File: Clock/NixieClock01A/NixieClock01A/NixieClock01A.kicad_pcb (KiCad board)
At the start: 2 copper layers, 17 parts, among them U1 74141, U2 PCF8574, U3 ESP-12E

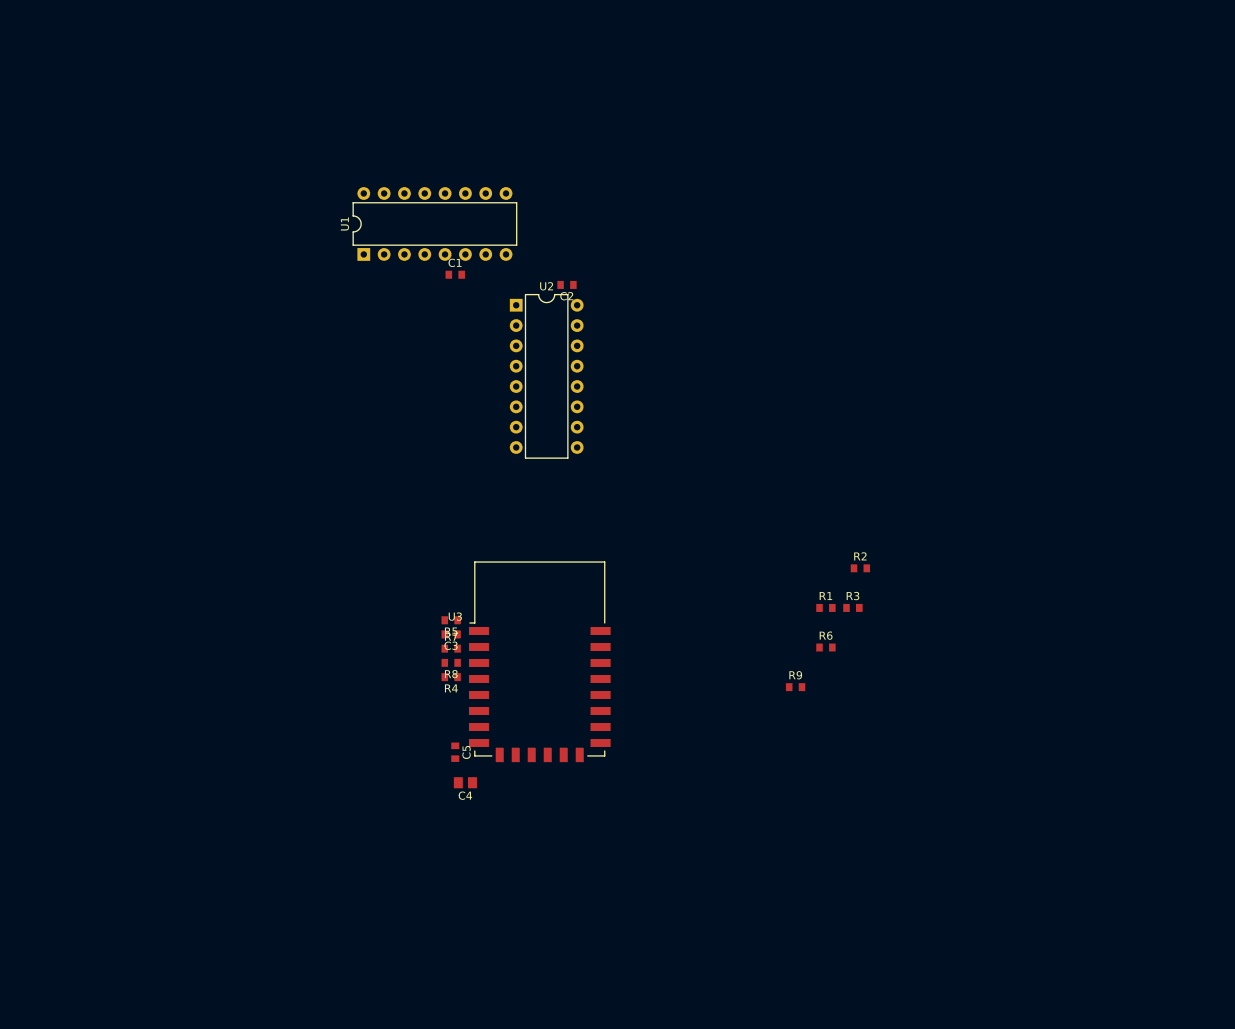
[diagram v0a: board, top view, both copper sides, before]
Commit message: LM3478, ESP8266 layout
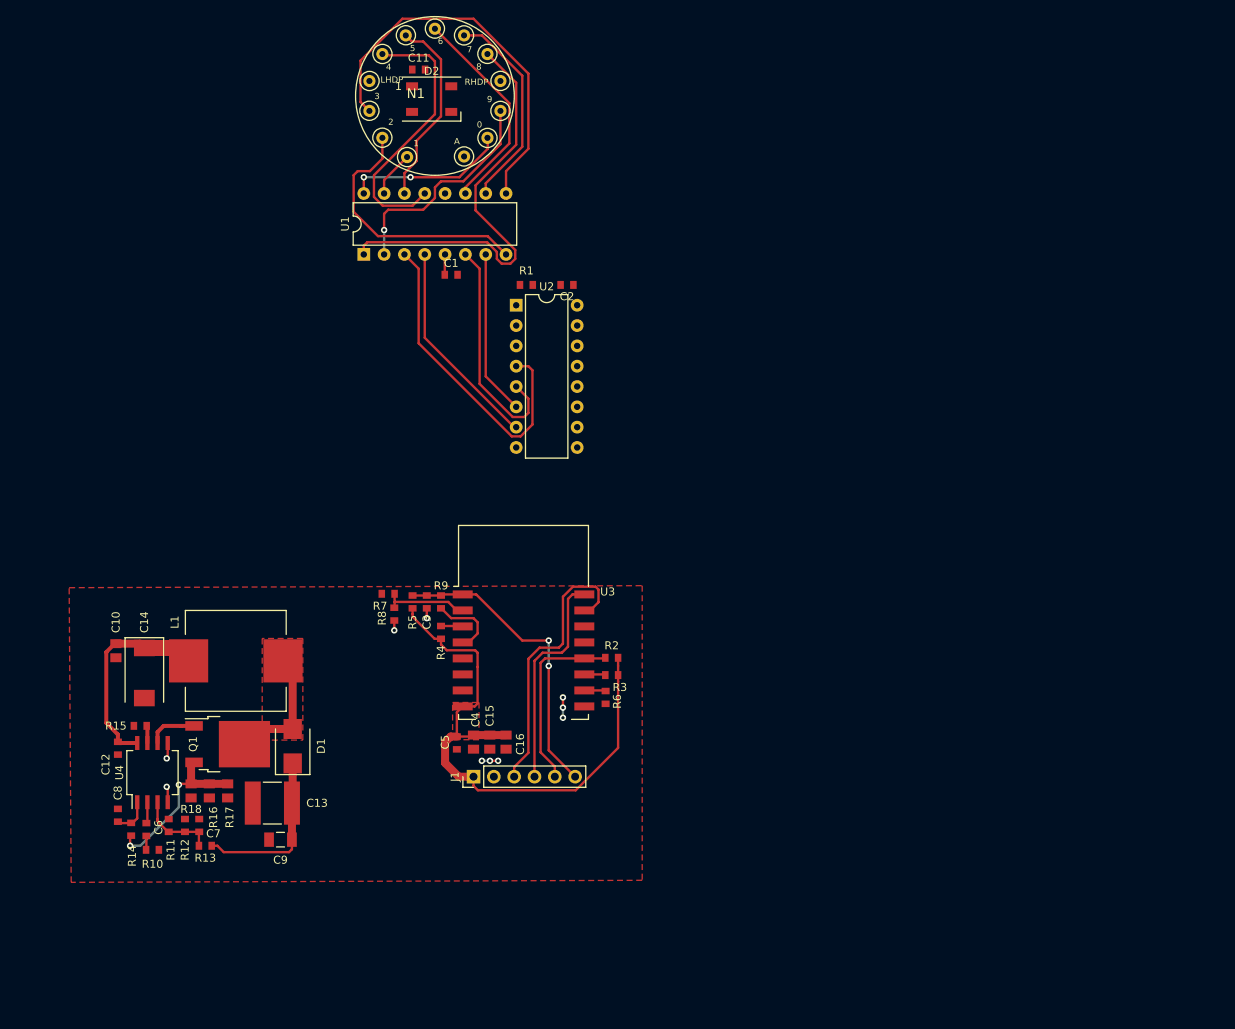
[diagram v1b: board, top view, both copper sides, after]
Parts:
- added C10: 10u, Capacitor_SMD:C_0805_2012Metric, F.Cu at (87.1, 106.7)
- added C11: 100n, Capacitor_SMD:C_0603_1608Metric, F.Cu at (125.0, 34.0)
- added C12: 100n, Capacitor_SMD:C_0603_1608Metric, F.Cu at (87.4, 118.9)
- added C13: 1u, Capacitor_SMD:C_2220_5650Metric, F.Cu at (106.7, 125.7)
- added C14: 100u, Capacitor_Tantalum_SMD:CP_EIA-7343-31_Kemet-D, F.Cu at (90.7, 109.5)
- added C15: 10u, Capacitor_SMD:C_0805_2012Metric, F.Cu at (133.9, 118.1)
- added C16: 10u, Capacitor_SMD:C_0805_2012Metric, F.Cu at (135.9, 118.1)
- added C6: 22n, Capacitor_SMD:C_0603_1608Metric, F.Cu at (90.9, 129.0)
- added C7: 22n, Capacitor_SMD:C_0603_1608Metric, F.Cu at (97.5, 128.5)
- added C8: C, Capacitor_SMD:C_0603_1608Metric, F.Cu at (87.4, 127.3)
- added C9: 100n, Capacitor_SMD:C_1206_3216Metric, F.Cu at (107.7, 130.3)
- added D1: D_Schottky, Diode_SMD:D_SMB, F.Cu at (109.2, 118.6)
- added D2: WS2812B, LED_SMD:LED_WS2812B_PLCC4_5.0x5.0mm_P3.2mm, F.Cu at (126.6, 37.7)
- added J1: Conn_01x06_Male, Connector_PinHeader_2.54mm:PinHeader_1x06_P2.54mm_Vertical, F.Cu at (131.8, 122.4)
- added L1: L_Core_Ferrite, Inductor_SMD:L_Wuerth_WE-PD-Typ-LS_Handsoldering, F.Cu at (102.1, 108.0)
- added N1: ZM1080, zm1080:ZM1080, F.Cu at (127.0, 37.3)
- added Q1: Q_NMOS_GDS, Package_TO_SOT_SMD:TO-252-2, F.Cu at (101.1, 118.4)
- added R10: 4k7, Resistor_SMD:R_0603_1608Metric, F.Cu at (91.7, 131.6)
- added R11: R, Resistor_SMD:R_0603_1608Metric, F.Cu at (93.7, 128.5)
- added R12: R, Resistor_SMD:R_0603_1608Metric, F.Cu at (95.8, 128.5)
- added R13: R, Resistor_SMD:R_0603_1608Metric, F.Cu at (98.3, 131.1)
- added R14: R, Resistor_SMD:R_0603_1608Metric, F.Cu at (89.0, 129.0)
- added R15: 40k, Resistor_SMD:R_0603_1608Metric, F.Cu at (90.2, 116.1)
- added R16: R, Resistor_SMD:R_0805_2012Metric, F.Cu at (98.8, 124.2)
- added R17: R, Resistor_SMD:R_0805_2012Metric, F.Cu at (101.1, 124.2)
- added R18: R, Resistor_SMD:R_0805_2012Metric, F.Cu at (96.5, 124.2)
- added U4: LM3478, Package_SO:SO-8_5.3x6.2mm_P1.27mm, F.Cu at (91.7, 121.9)
- U3: footprint RF_Module:ESP-12E -> riske-lib:ESP-12E
- moved R1 55.1 mm to (138.4, 61.0), turned to 180 degrees
- moved R9 45.6 mm to (127.8, 100.6), turned to 270 degrees
- moved R2 33.0 mm to (149.1, 107.6)
- moved R3 31.3 mm to (149.1, 109.7)
- moved R6 28.2 mm to (148.3, 112.5), turned to 270 degrees
- moved R7 10.4 mm to (121.2, 99.6)
- moved R8 9.37 mm to (121.9, 102.1), turned to 270 degrees
- moved R4 5.73 mm to (127.8, 104.4), turned to 270 degrees
- moved R5 5.34 mm to (124.2, 100.6), turned to 270 degrees
- moved C4 5.18 mm to (131.8, 118.1), turned to 270 degrees
- moved C3 5.08 mm to (126.0, 100.6), turned to 270 degrees
- moved U3 5.00 mm to (138.1, 103.1)
- moved C5 1.19 mm to (129.7, 118.2)
- moved C1 0.51 mm to (129.0, 59.7)
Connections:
- U3 pad 21: Net-(U3-Pad21) -> /RX
- U3 pad 22: Net-(U3-Pad22) -> /TX
- U3 pad 7: Net-(U3-Pad7) -> /NeoPix1
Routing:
- net +3V3: track 0.00 -> 71.7 mm
- net Net-(N1-Pad9): track 0.00 -> 53.3 mm
- net Net-(N1-Pad3): track 0.00 -> 48.9 mm
- net /A1: track 0.00 -> 40.5 mm
- net /RST: track 0.00 -> 37.8 mm, vias 0 -> 2
- net /RX: track 0.00 -> 35.3 mm
- net Net-(N1-Pad5): track 0.00 -> 34.5 mm
- net Net-(N1-Pad2): track 0.00 -> 32.9 mm
- net /A2: track 0.00 -> 28.9 mm
- net +5V: track 0.00 -> 28.5 mm
- net Net-(N1-Pad11): track 0.00 -> 28.2 mm, vias 0 -> 1
- net /TX: track 0.00 -> 27.6 mm
- net Net-(N1-Pad7): track 0.00 -> 26.7 mm
- net /A4: track 0.00 -> 26.5 mm
- net Net-(N1-Pad8): track 0.00 -> 26.0 mm
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- added copper zone on F.Cu, net +3V3
- added copper zone on F.Cu, net GND
- added copper zone on F.Cu, net Net-(D1-Pad2)
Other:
- net class Default: trace_width 0.25 -> 0.2
- rule via_min_size: 0.4 -> 0.5

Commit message: Nixie layout
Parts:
- added C17: 100n, Capacitor_SMD:C_0603_1608Metric, B.Cu at (193.0, 83.2)
- added C18: 100n, Capacitor_SMD:C_0603_1608Metric, F.Cu at (139.0, 142.0)
- added C19: 100n, Capacitor_SMD:C_0603_1608Metric, F.Cu at (189.6, 62.8)
- added C20: 100n, Capacitor_SMD:C_0603_1608Metric, F.Cu at (158.8, 62.8)
- added C21: 100n, Capacitor_SMD:C_0603_1608Metric, F.Cu at (125.5, 142.0)
- added C22: 100n, Capacitor_SMD:C_0603_1608Metric, B.Cu at (162.2, 83.2)
- added C23: 100n, Capacitor_SMD:C_0603_1608Metric, F.Cu at (137.4, 62.8)
- added C24: 100n, Capacitor_SMD:C_0603_1608Metric, F.Cu at (106.2, 62.8)
- added C25: 10u, Capacitor_SMD:C_0805_2012Metric, F.Cu at (156.0, 119.8)
- added C26: 10u, Capacitor_SMD:C_0805_2012Metric, F.Cu at (146.0, 123.5)
- added C27: 100n, Capacitor_SMD:C_0603_1608Metric, B.Cu at (140.8, 83.2)
- added C28: 100n, Capacitor_SMD:C_0603_1608Metric, F.Cu at (84.8, 62.8)
- added C29: 100n, Capacitor_SMD:C_0603_1608Metric, F.Cu at (156.0, 123.2)
- added C30: 100n, Capacitor_SMD:C_0603_1608Metric, F.Cu at (146.0, 119.5)
- added C31: 100n, Capacitor_SMD:C_0603_1608Metric, B.Cu at (109.8, 83.2)
- added C32: 100n, Capacitor_SMD:C_0603_1608Metric, B.Cu at (88.2, 83.2)
- added D3: WS2812B, LED_SMD:LED_WS2812B_PLCC4_5.0x5.0mm_P3.2mm, F.Cu at (191.5, 66.4)
- added D4: WS2812B, LED_SMD:LED_WS2812B_PLCC4_5.0x5.0mm_P3.2mm, F.Cu at (161.0, 66.4)
- added D5: WS2812B, LED_SMD:LED_WS2812B_PLCC4_5.0x5.0mm_P3.2mm, F.Cu at (139.6, 66.5)
- added D6: WS2812B, LED_SMD:LED_WS2812B_PLCC4_5.0x5.0mm_P3.2mm, F.Cu at (108.5, 66.4)
- added D7: WS2812B, LED_SMD:LED_WS2812B_PLCC4_5.0x5.0mm_P3.2mm, F.Cu at (87.0, 66.4)
- added J2: Conn_02x16_Odd_Even, Connector_PinSocket_2.54mm:PinSocket_2x16_P2.54mm_Vertical, F.Cu at (170.0, 149.0)
- added J3: Conn_02x16_Odd_Even, Connector_PinSocket_2.54mm:PinSocket_2x16_P2.54mm_Vertical, F.Cu at (170.0, 97.0)
- added N2: ZM1080, riske-lib:ZM1080, F.Cu at (191.5, 66.3)
- added N3: ZM1080, riske-lib:ZM1080, F.Cu at (161.0, 66.3)
- added N4: ZM1080, riske-lib:ZM1080, F.Cu at (139.6, 66.4)
- added N5: ZM1080, riske-lib:ZM1080, F.Cu at (108.5, 66.3)
- added N6: ZM1080, riske-lib:ZM1080, F.Cu at (87.0, 66.3)
- added R19: R, Resistor_SMD:R_0603_1608Metric, F.Cu at (150.0, 140.0)
- added R20: R, Resistor_SMD:R_0603_1608Metric, F.Cu at (136.5, 140.0)
- added R21: 27k, Resistor_SMD:R_1206_3216Metric, B.Cu at (213.2, 75.0)
- added R22: 27k, Resistor_SMD:R_1206_3216Metric, B.Cu at (191.6, 75.0)
- added R23: 27k, Resistor_SMD:R_1206_3216Metric, B.Cu at (161.2, 75.0)
- added R24: 27k, Resistor_SMD:R_1206_3216Metric, B.Cu at (139.8, 75.2)
- added R25: 27k, Resistor_SMD:R_1206_3216Metric, B.Cu at (108.6, 75.0)
- added R26: 27k, Resistor_SMD:R_1206_3216Metric, B.Cu at (87.0, 75.0)
- added U10: L78L33_TO92, Package_TO_SOT_THT:TO-92_Inline, F.Cu at (149.9, 120.3)
- added U11: 74141, Package_DIP:DIP-16_W7.62mm, F.Cu at (130.6, 86.0)
- added U12: 74141, Package_DIP:DIP-16_W7.62mm, F.Cu at (99.5, 85.9)
- added U13: 74141, Package_DIP:DIP-16_W7.62mm, F.Cu at (78.0, 85.9)
- added U5: 74141, Package_DIP:DIP-16_W7.62mm, F.Cu at (182.8, 85.9)
- added U6: PCF8574, Package_SO:SOIC-16W_5.3x10.2mm_P1.27mm, F.Cu at (144.0, 136.0)
- added U7: PCF8574, Package_SO:SOIC-16W_5.3x10.2mm_P1.27mm, F.Cu at (130.5, 136.0)
- added U8: 74141, Package_DIP:DIP-16_W7.62mm, F.Cu at (152.0, 85.9)
- added U9: L78L05_TO92, Package_TO_SOT_THT:TO-92_Inline, F.Cu at (159.3, 120.0)
- C1: moved to B.Cu
- C13: value 1u -> 1u/200V
- C9: value 100n -> 100n/200V
- N1: footprint zm1080:ZM1080 -> riske-lib:ZM1080
- U2: footprint Package_DIP:DIP-16_W7.62mm -> Package_SO:SOIC-16W_5.3x10.2mm_P1.27mm
- U3: footprint riske-lib:ESP-12E -> RF_Module:ESP-12E
- moved C10 108.7 mm to (194.8, 121.4), turned to 180 degrees
- moved C14 102.5 mm to (192.0, 124.9), turned to 180 degrees
- moved L1 95.8 mm to (193.6, 136.4), turned to 270 degrees
- moved R15 95.6 mm to (185.4, 124.4), turned to 90 degrees
- moved C12 95.3 mm to (182.6, 121.6), turned to 180 degrees
- moved D2 91.0 mm to (213.0, 66.4)
- moved N1 90.7 mm to (213.0, 66.3)
- moved C11 90.7 mm to (211.0, 62.8)
- moved U1 90.7 mm to (204.1, 85.9)
- moved C1 88.4 mm to (214.3, 83.2), turned to 90 degrees
- moved U4 88.0 mm to (179.6, 125.9), turned to 0 degrees
- moved C8 87.1 mm to (174.2, 121.6), turned to 180 degrees
- moved Q1 83.8 mm to (183.1, 135.3), turned to 270 degrees
- moved R14 83.7 mm to (172.5, 123.3), turned to 0 degrees
- moved R1 82.8 mm to (163.0, 140.0), turned to 270 degrees
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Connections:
- net /NeoPix1 renamed /NeoPix
- C11 pad 1: +3V3 -> +5V
- D2 pad 1: +3V3 -> +5V
- J1 pad 1: +3V3 -> GND
- J1 pad 2: GND -> +3V3
- J1 pad 3: /RX -> /TX
- J1 pad 4: /TX -> /RX
- N1 pad 13: /Uanode -> Net-(N1-Pad13)
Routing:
- net +5V: track 28.5 -> 349.2 mm, vias 0 -> 6
- net /Uanode: track 21.3 -> 273.6 mm, vias 0 -> 1
- net /F3: track 0.00 -> 86.6 mm
- net /NeoPix: track 0.00 -> 85.3 mm, vias 0 -> 1
- net /F4: track 0.00 -> 80.0 mm
- net /F1: track 0.00 -> 74.3 mm
- net /E3: track 0.00 -> 73.7 mm
- net /F2: track 0.00 -> 72.6 mm
- net /E4: track 0.00 -> 68.8 mm
- net /B3: track 0.00 -> 67.7 mm
- net /B2: track 0.00 -> 66.3 mm
- net /A3: track 20.6 -> 83.2 mm
- net /B4: track 0.00 -> 62.5 mm
- net Net-(N2-Pad2): track 0.00 -> 55.2 mm
- net /A4: track 26.5 -> 81.4 mm
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- added copper zone on B.Cu, net GND
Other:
- net class Default: trace_width 0.2 -> 0.3
